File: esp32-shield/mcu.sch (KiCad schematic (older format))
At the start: 27 parts, among them J11 DNP, J5 Conn_01x14_Female, J6 Conn_01x14_Female, Q3 S8050, Q4 S8050, SW1 DNP, U13 ESP32-WROOM32, U14 W25Q32JVSS, U5 CH340C, U6 AMS1117-3.3, Y1 12MHZ

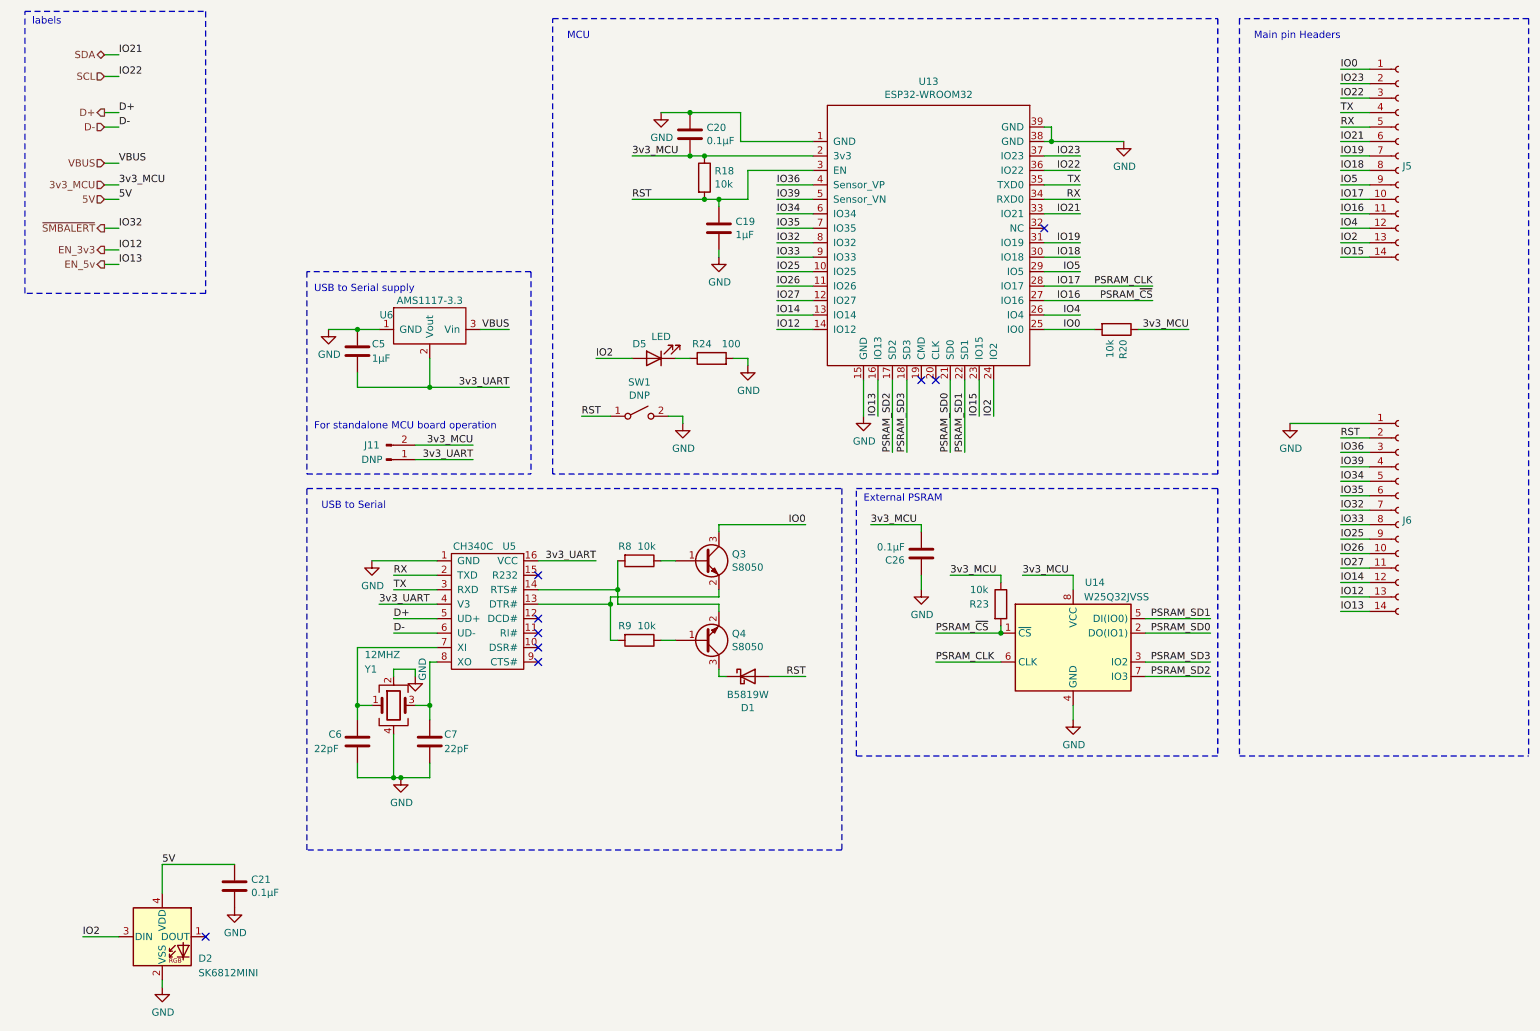
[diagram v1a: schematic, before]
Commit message: added more input caps & part number for button
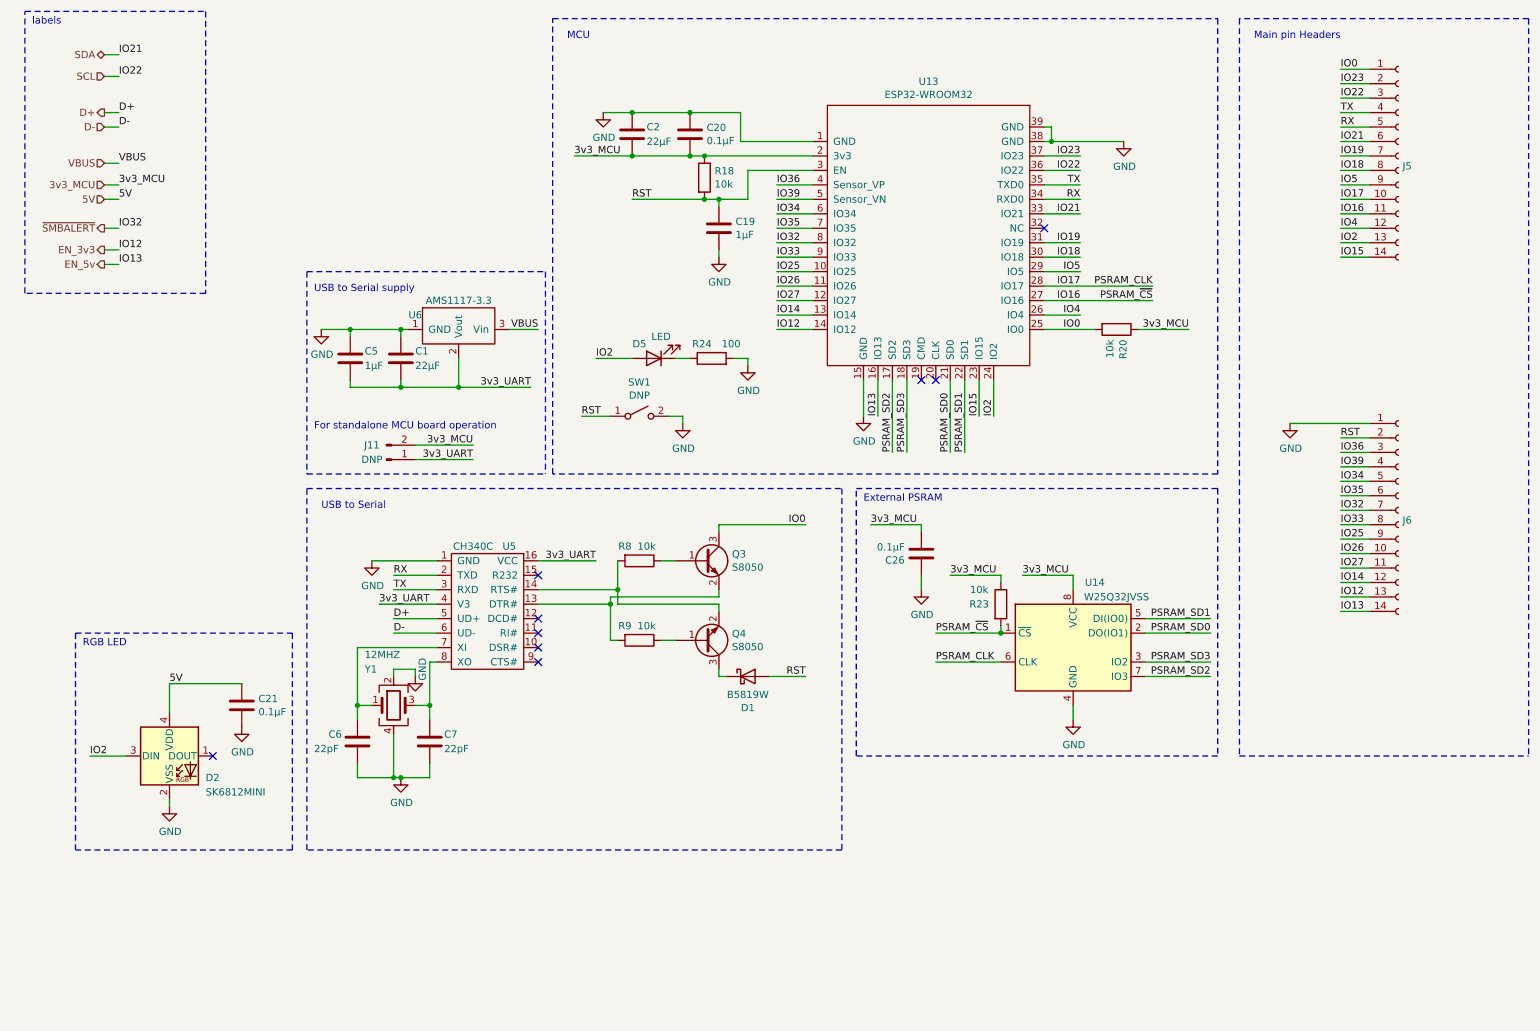
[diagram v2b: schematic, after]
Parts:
- added C1, C2: 22µF, Capacitor_SMD:C_0805_2012Metric, symbol Device:C
- SW1: LCSC (none) -> C231329
- U14: LCSC (none) -> C25804
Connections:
- net 3v3_MCU: now also C2.2
- net 3v3_UART: now also C1.2
- net GND: now also C1.1, C2.1
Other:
- note added: "RGB LED"
- moved on the sheet: C21, C5, D2, U6
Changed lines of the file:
@@
 L power:GND #PWR0116
 U 1 1 5F82BD5E
-P 5000 1350
-F 0 "#PWR0116" H 5000 1100 50  0001 C CNN
-F 1 "GND" H 5005 1177 50  0000 C CNN
-F 2 "" H 5000 1350 50  0001 C CNN
-F 3 "" H 5000 1350 50  0001 C CNN
-	1    5000 1350
-	1    0    0    -1
-$EndComp
-Wire Wire Line
-	5000 1350 5200 1350
+P 4600 1350
+F 0 "#PWR0116" H 4600 1100 50  0001 C CNN
+F 1 "GND" H 4605 1177 50  0000 C CNN
+F 2 "" H 4600 1350 50  0001 C CNN
+F 3 "" H 4600 1350 50  0001 C CNN
+	1    4600 1350
+	1    0    0    -1
+$EndComp
 Connection ~ 5200 1350
 Wire Notes Line
@@
 Text Notes 4350 850  0    50   ~ 0
 MCU
-Text Label 4800 1650 0    50   ~ 0
+Text Label 4400 1650 0    50   ~ 0
 3v3_MCU
-Wire Wire Line
-	4800 1650 5200 1650
 Wire Wire Line
 	1150 1850 1250 1850
@@
 L AMS1117-3.3:AMS1117-3.3 U?
 U 1 1 5FEC8BE4
-P 3400 2800
+P 3600 2800
 AR Path="/5F63B107/5FEC8BE4" Ref="U?"  Part="1"
 AR Path="/5F63A193/5FEC8BE4" Ref="U6"  Part="1"
-F 0 "U6" H 3100 2850 50  0000 C CNN
-F 1 "AMS1117-3.3" H 3400 2950 50  0000 C CNN
-F 2 "Package_TO_SOT_SMD:SOT-223-3_TabPin2" H 3700 2500 50  0001 C CNN
-F 3 "http://www.advanced-monolithic.com/pdf/ds1117.pdf" H 3600 2850 50  0001 C CNN
-F 4 "C6186" H 3400 2800 50  0001 C CNN "LCSC"
-	1    3400 2800
+F 0 "U6" H 3300 2850 50  0000 C CNN
+F 1 "AMS1117-3.3" H 3600 2950 50  0000 C CNN
+F 2 "Package_TO_SOT_SMD:SOT-223-3_TabPin2" H 3900 2500 50  0001 C CNN
+F 3 "http://www.advanced-monolithic.com/pdf/ds1117.pdf" H 3800 2850 50  0001 C CNN
+F 4 "C6186" H 3600 2800 50  0001 C CNN "LCSC"
+	1    3600 2800
 	1    0    0    -1
 $EndComp
@@
 $EndComp
 Wire Wire Line
-	3400 3050 3400 3250
-Text Label 3950 3250 2    50   ~ 0
+	3600 3050 3600 3250
+Text Label 4100 3250 2    50   ~ 0
 3v3_UART
-Text Label 3950 2850 2    50   ~ 0
+Text Label 4150 2850 2    50   ~ 0
 VBUS
 Wire Wire Line
-	3750 2850 3950 2850
+	3950 2850 4150 2850
 Wire Wire Line
 	3000 4450 3450 4450
@@
 L power:GND #PWR?
 U 1 1 5FEC8BFE
-P 2700 2850
+P 2650 2850
 AR Path="/5F63B107/5FEC8BFE" Ref="#PWR?"  Part="1"
 AR Path="/5F63A193/5FEC8BFE" Ref="#PWR0125"  Part="1"
-F 0 "#PWR0125" H 2700 2600 50  0001 C CNN
-F 1 "GND" H 2705 2677 50  0000 C CNN
-F 2 "" H 2700 2850 50  0001 C CNN
-F 3 "" H 2700 2850 50  0001 C CNN
-	1    2700 2850
+F 0 "#PWR0125" H 2650 2600 50  0001 C CNN
+F 1 "GND" H 2655 2677 50  0000 C CNN
+F 2 "" H 2650 2850 50  0001 C CNN
+F 3 "" H 2650 2850 50  0001 C CNN
+	1    2650 2850
 	1    0    0    -1
 $EndComp
@@
 Wire Notes Line
 	2550 6450 2550 3950
-Wire Notes Line
-	4100 2450 2550 2450
-Wire Notes Line
-	2550 3850 4100 3850
 Text Notes 2600 2600 0    50   ~ 0
 USB to Serial supply\n
@@
 Text Label 3150 4550 0    50   ~ 0
 RX
-Wire Wire Line
-	3050 2850 2900 2850
-Wire Wire Line
-	2900 2850 2700 2850
-Connection ~ 2900 2850
 $Comp
 L Device:C C?
 U 1 1 5FEC8C26
-P 2900 3000
+P 2850 3050
 AR Path="/5F63B107/5FEC8C26" Ref="C?"  Part="1"
 AR Path="/5F63A193/5FEC8C26" Ref="C5"  Part="1"
-F 0 "C5" H 3000 3050 50  0000 L CNN
-F 1 "1µF" H 3000 2950 50  0000 L CNN
-F 2 "Capacitor_SMD:C_0603_1608Metric_Pad1.05x0.95mm_HandSolder" H 2938 2850 50  0001 C CNN
-F 3 "~" H 2900 3000 50  0001 C CNN
-F 4 "C15849" H 2900 3000 50  0001 C CNN "LCSC"
-	1    2900 3000
-	1    0    0    -1
-$EndComp
-Wire Wire Line
-	2900 3150 2900 3250
-Wire Wire Line
-	2900 3250 3400 3250
-Connection ~ 3400 3250
+F 0 "C5" H 2950 3100 50  0000 L CNN
+F 1 "1µF" H 2950 3000 50  0000 L CNN
+F 2 "Capacitor_SMD:C_0603_1608Metric_Pad1.05x0.95mm_HandSolder" H 2888 2900 50  0001 C CNN
+F 3 "~" H 2850 3050 50  0001 C CNN
+F 4 "C15849" H 2850 3050 50  0001 C CNN "LCSC"
+	1    2850 3050
+	1    0    0    -1
+$EndComp
 $Comp
 L Transistor_BJT:BC817 Q?
@@
 Wire Wire Line
 	1150 2150 1250 2150
-Wire Wire Line
-	3400 3250 3950 3250
 $Comp
 L Switch:SW_SPST SW1
@@
 F 2 "Button_Switch_SMD:SW_Push_SPST_NO_Alps_SKRK" H 4850 3450 50  0001 C CNN
 F 3 "~" H 4850 3450 50  0001 C CNN
+F 4 "C231329" H 4850 3450 50  0001 C CNN "LCSC"
 	1    4850 3450
 	1    0    0    -1
@@
 	2550 2450 2550 3850
 Wire Notes Line
-	4100 2450 4100 3850
+	4200 2450 4200 3850
 Text Notes 2600 3550 0    50   ~ 0
 For standalone MCU board operation
@@
 F 3 "http://www.winbond.com/resource-files/w25q32jv%20revg%2003272018%20plus.pdf" H 7850 5050 50  0001 C CNN
 F 4 "DNP" H 7850 5050 50  0001 C CNN "DNP"
+F 5 "C25804" H 7850 5050 50  0001 C CNN "LCSC"
 	1    7850 5050
 	1    0    0    -1
@@
 L LED:SK6812MINI D2
 U 1 1 60359CD9
-P 1550 7050
-F 0 "D2" H 1800 6900 50  0000 L CNN
-F 1 "SK6812MINI" H 1800 6800 50  0000 L CNN
-F 2 "LED_SMD:LED_SK6812MINI_PLCC4_3.5x3.5mm_P1.75mm" H 1600 6750 50  0001 L TNN
-F 3 "https://cdn-shop.adafruit.com/product-files/2686/SK6812MINI_REV.01-1-2.pdf" H 1650 6675 50  0001 L TNN
-	1    1550 7050
+P 1600 5800
+F 0 "D2" H 1850 5650 50  0000 L CNN
+F 1 "SK6812MINI" H 1850 5550 50  0000 L CNN
+F 2 "LED_SMD:LED_SK6812MINI_PLCC4_3.5x3.5mm_P1.75mm" H 1650 5500 50  0001 L TNN
+F 3 "https://cdn-shop.adafruit.com/product-files/2686/SK6812MINI_REV.01-1-2.pdf" H 1700 5425 50  0001 L TNN
+	1    1600 5800
 	1    0    0    -1
 $EndComp
@@
 Text Label 1250 1950 0    50   ~ 0
 5V
-Text Label 1550 6550 0    50   ~ 0
+Text Label 1600 5300 0    50   ~ 0
 5V
 $Comp
 L Device:C C21
 U 1 1 603835DD
-P 2050 6700
-F 0 "C21" H 2165 6746 50  0000 L CNN
-F 1 "0.1µF" H 2165 6655 50  0000 L CNN
-F 2 "Capacitor_SMD:C_0603_1608Metric_Pad1.05x0.95mm_HandSolder" H 2088 6550 50  0001 C CNN
-F 3 "~" H 2050 6700 50  0001 C CNN
-F 4 "C14858" H 2050 6700 50  0001 C CNN "LCSC"
-	1    2050 6700
+P 2100 5450
+F 0 "C21" H 2215 5496 50  0000 L CNN
+F 1 "0.1µF" H 2215 5405 50  0000 L CNN
+F 2 "Capacitor_SMD:C_0603_1608Metric_Pad1.05x0.95mm_HandSolder" H 2138 5300 50  0001 C CNN
+F 3 "~" H 2100 5450 50  0001 C CNN
+F 4 "C14858" H 2100 5450 50  0001 C CNN "LCSC"
+	1    2100 5450
 	1    0    0    -1
 $EndComp
@@
 L power:GND #PWR?
 U 1 1 603847FA
-P 1550 7400
+P 1600 6150
 AR Path="/5F63B107/603847FA" Ref="#PWR?"  Part="1"
 AR Path="/5F63A193/603847FA" Ref="#PWR0101"  Part="1"
-F 0 "#PWR0101" H 1550 7150 50  0001 C CNN
-F 1 "GND" H 1555 7227 50  0000 C CNN
-F 2 "" H 1550 7400 50  0001 C CNN
-F 3 "" H 1550 7400 50  0001 C CNN
-	1    1550 7400
+F 0 "#PWR0101" H 1600 5900 50  0001 C CNN
+F 1 "GND" H 1605 5977 50  0000 C CNN
+F 2 "" H 1600 6150 50  0001 C CNN
+F 3 "" H 1600 6150 50  0001 C CNN
+	1    1600 6150
 	1    0    0    -1
 $EndComp
@@
 L power:GND #PWR?
 U 1 1 60385656
-P 2050 6850
+P 2100 5600
 AR Path="/5F63B107/60385656" Ref="#PWR?"  Part="1"
 AR Path="/5F63A193/60385656" Ref="#PWR0102"  Part="1"
-F 0 "#PWR0102" H 2050 6600 50  0001 C CNN
-F 1 "GND" H 2055 6677 50  0000 C CNN
-F 2 "" H 2050 6850 50  0001 C CNN
-F 3 "" H 2050 6850 50  0001 C CNN
-	1    2050 6850
-	1    0    0    -1
-$EndComp
-Wire Wire Line
-	2050 6550 1550 6550
-Wire Wire Line
-	1550 6550 1550 6750
-Wire Wire Line
-	1250 7050 1000 7050
-NoConn ~ 1850 7050
+F 0 "#PWR0102" H 2100 5350 50  0001 C CNN
+F 1 "GND" H 2105 5427 50  0000 C CNN
+F 2 "" H 2100 5600 50  0001 C CNN
+F 3 "" H 2100 5600 50  0001 C CNN
+	1    2100 5600
+	1    0    0    -1
+$EndComp
+Wire Wire Line
+	2100 5300 1600 5300
+Wire Wire Line
+	1600 5300 1600 5500
+Wire Wire Line
+	1300 5800 1050 5800
+NoConn ~ 1900 5800
 Text Label 7300 3450 1    50   ~ 0
 IO2
 Wire Wire Line
 	7300 3450 7300 3200
-Text Label 1000 7050 0    50   ~ 0
+Text Label 1050 5800 0    50   ~ 0
 IO2
 Wire Wire Line
-	1550 7350 1550 7400
+	1600 6100 1600 6150
+$Comp
+L Device:C C?
+U 1 1 6044C2AF
+P 3200 3050
+AR Path="/5F63B107/6044C2AF" Ref="C?"  Part="1"
+AR Path="/5F63A193/6044C2AF" Ref="C1"  Part="1"
+F 0 "C1" H 3300 3100 50  0000 L CNN
+F 1 "22µF" H 3300 3000 50  0000 L CNN
+F 2 "Capacitor_SMD:C_0805_2012Metric" H 3238 2900 50  0001 C CNN
+F 3 "~" H 3200 3050 50  0001 C CNN
+F 4 "C45783" H 3200 3050 50  0001 C CNN "LCSC"
+	1    3200 3050
+	1    0    0    -1
+$EndComp
+Wire Notes Line
+	2550 2450 4200 2450
+Wire Notes Line
+	2550 3850 4200 3850
+Connection ~ 3600 3250
+Wire Wire Line
+	3600 3250 4100 3250
+Wire Wire Line
+	2850 3250 3200 3250
+Wire Wire Line
+	2850 3200 2850 3250
+Wire Wire Line
+	2650 2850 2850 2850
+Wire Wire Line
+	2850 2900 2850 2850
+Connection ~ 2850 2850
+Wire Wire Line
+	2850 2850 3200 2850
+Wire Wire Line
+	3200 2900 3200 2850
+Connection ~ 3200 2850
+Wire Wire Line
+	3200 2850 3250 2850
+Wire Wire Line
+	3200 3200 3200 3250
+Connection ~ 3200 3250
+Wire Wire Line
+	3200 3250 3600 3250
+Connection ~ 4800 1350
+Wire Wire Line
+	4800 1350 5200 1350
+Connection ~ 4800 1650
+Wire Wire Line
+	4800 1650 5200 1650
+Wire Wire Line
+	4400 1650 4800 1650
+Wire Wire Line
+	4600 1350 4800 1350
+$Comp
+L Device:C C?
+U 1 1 605156CE
+P 4800 1500
+AR Path="/5F63B107/605156CE" Ref="C?"  Part="1"
+AR Path="/5F63A193/605156CE" Ref="C2"  Part="1"
+F 0 "C2" H 4900 1550 50  0000 L CNN
+F 1 "22µF" H 4900 1450 50  0000 L CNN
+F 2 "Capacitor_SMD:C_0805_2012Metric" H 4838 1350 50  0001 C CNN
+F 3 "~" H 4800 1500 50  0001 C CNN
+F 4 "C45783" H 4800 1500 50  0001 C CNN "LCSC"
+	1    4800 1500
+	1    0    0    -1
+$EndComp
+Wire Notes Line
+	950  4950 2450 4950
+Wire Notes Line
+	2450 4950 2450 6450
+Wire Notes Line
+	2450 6450 950  6450
+Wire Notes Line
+	950  4950 950  6450
+Text Notes 1000 5050 0    50   ~ 0
+RGB LED
 $EndSCHEMATC

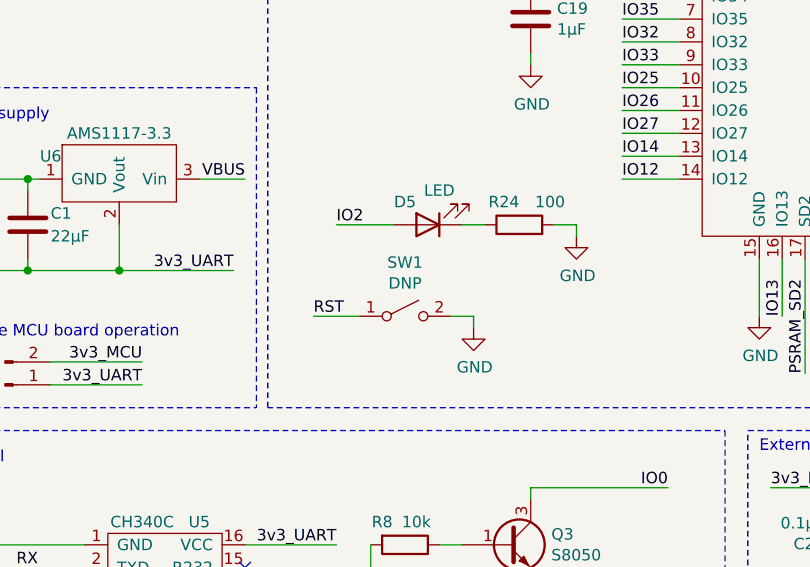
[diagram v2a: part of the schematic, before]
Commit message: changed switch value
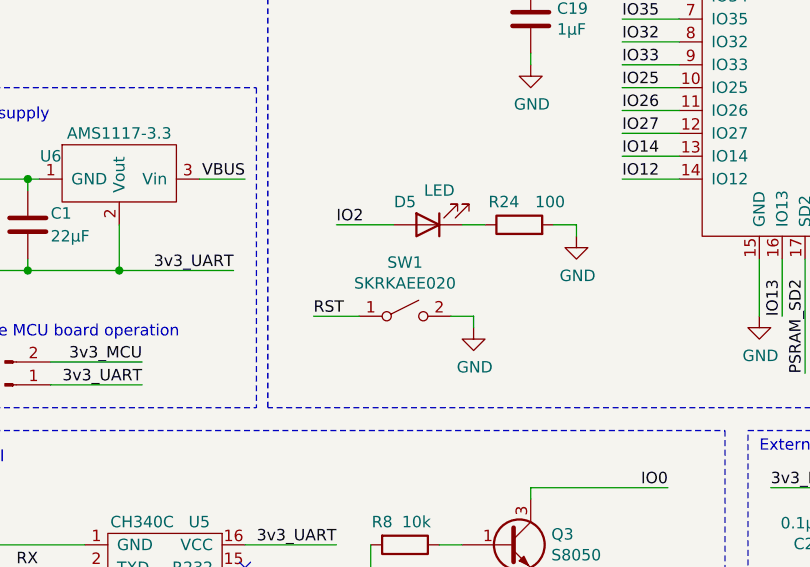
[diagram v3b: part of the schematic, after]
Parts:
- SW1: value DNP -> SKRKAEE020
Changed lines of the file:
@@
 P 4850 3450
 F 0 "SW1" H 4850 3685 50  0000 C CNN
-F 1 "DNP" H 4850 3594 50  0000 C CNN
+F 1 "SKRKAEE020" H 4850 3594 50  0000 C CNN
 F 2 "Button_Switch_SMD:SW_Push_SPST_NO_Alps_SKRK" H 4850 3450 50  0001 C CNN
 F 3 "~" H 4850 3450 50  0001 C CNN

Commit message: swapped button lcsc part number for cheaper alps one
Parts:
- SW1: LCSC C231329 -> C115357
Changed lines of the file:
@@
 F 2 "Button_Switch_SMD:SW_Push_SPST_NO_Alps_SKRK" H 4850 3450 50  0001 C CNN
 F 3 "~" H 4850 3450 50  0001 C CNN
-F 4 "C231329" H 4850 3450 50  0001 C CNN "LCSC"
+F 4 "C115357" H 4850 3450 50  0001 C CNN "LCSC"
 	1    4850 3450
 	1    0    0    -1
